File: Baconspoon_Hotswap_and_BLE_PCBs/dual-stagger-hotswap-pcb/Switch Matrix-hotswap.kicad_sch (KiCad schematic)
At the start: 87 parts

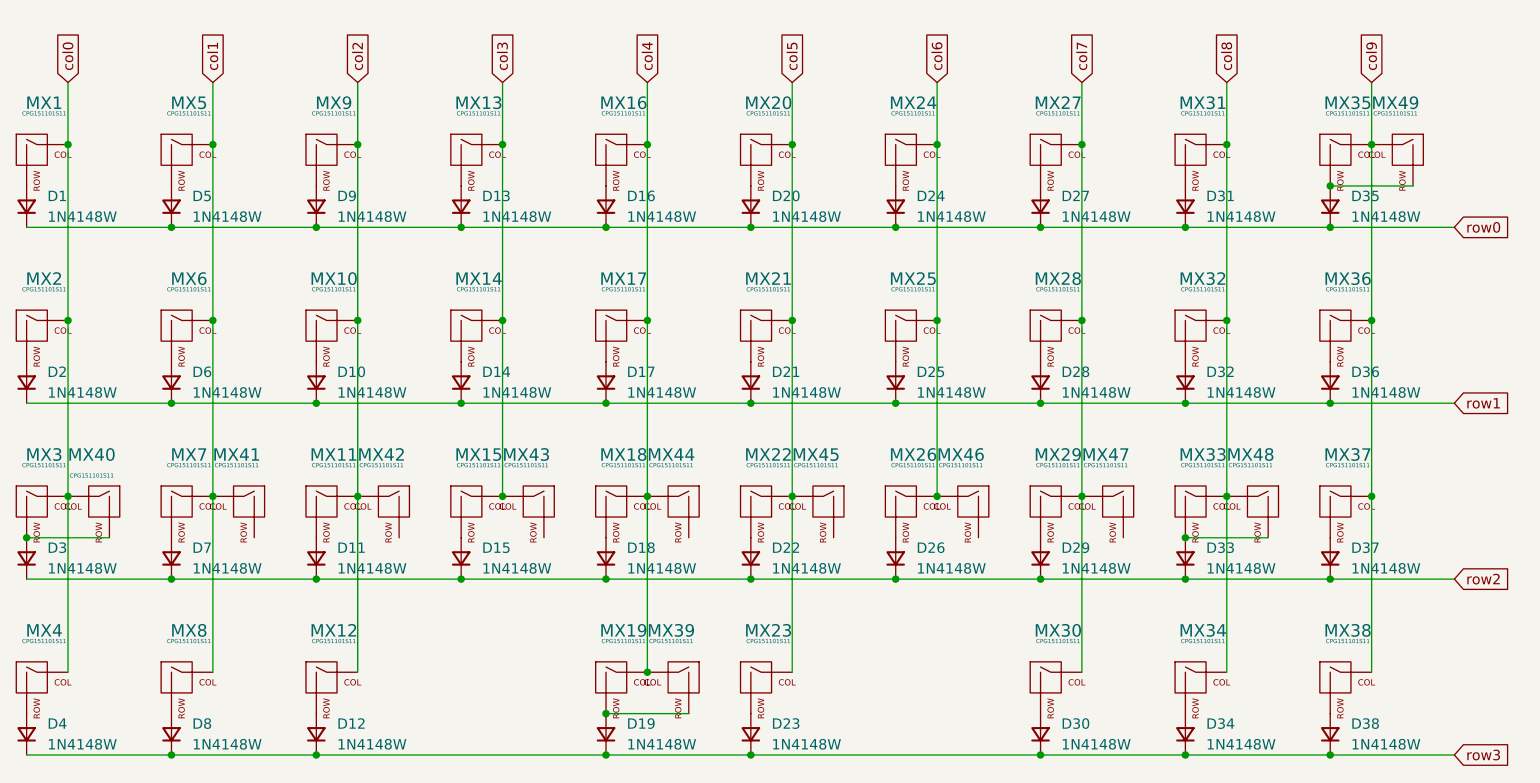
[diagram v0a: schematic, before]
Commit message: upload accurate fabrication files for dual-stagger hotswap PCB
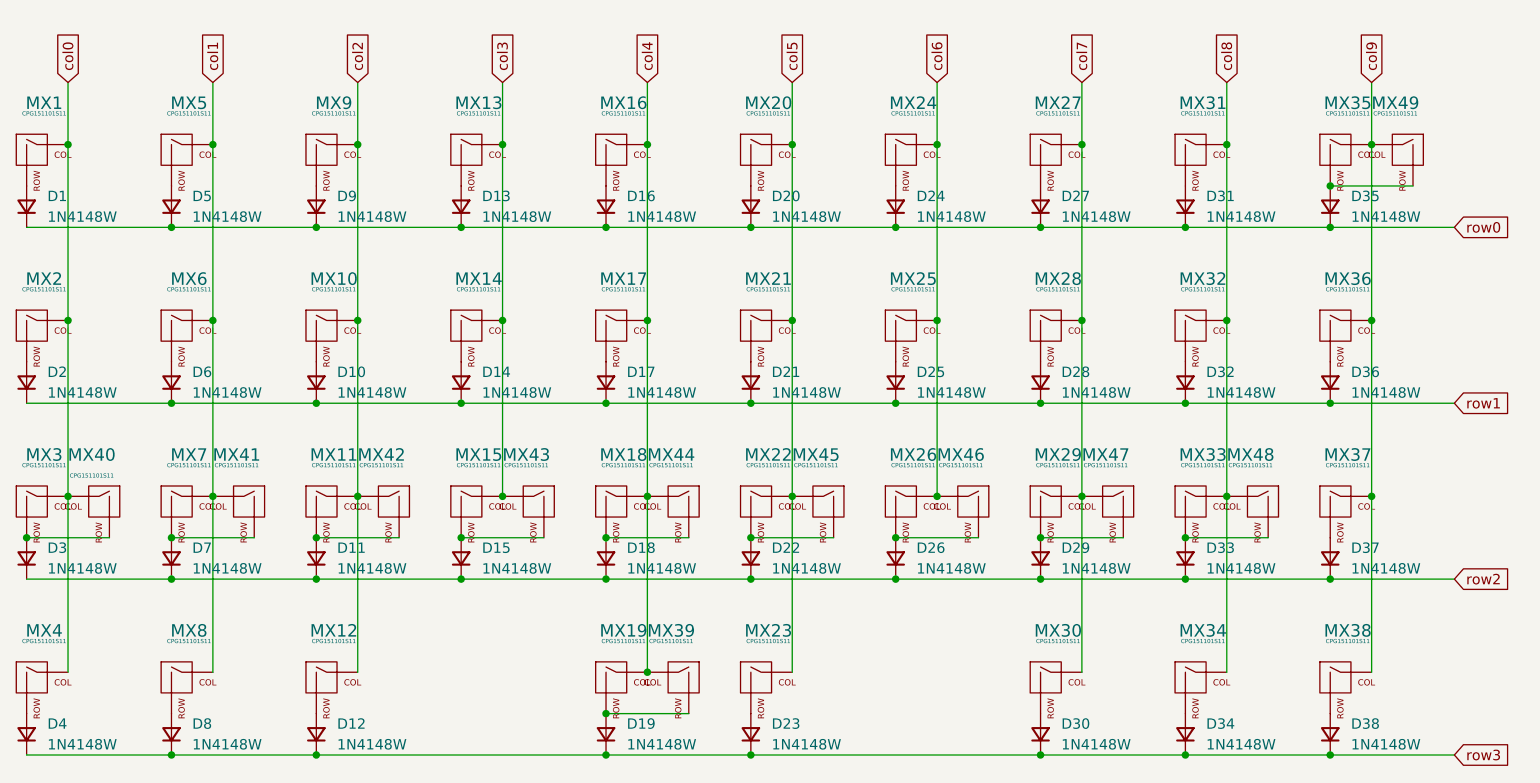
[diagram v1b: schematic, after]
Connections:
- net at D11.2 (A), MX11.2 (ROW): now also MX42.2 (ROW)
- net at D18.2 (A), MX18.2 (ROW): now also MX44.2 (ROW)
- net at D26.2 (A), MX26.2 (ROW): now also MX46.2 (ROW)
- net at MX47.2 (ROW): now also D29.2 (A), MX29.2 (ROW)
- net at MX41.2 (ROW): now also D7.2 (A), MX7.2 (ROW)
- net at D22.2 (A), MX22.2 (ROW): now also MX45.2 (ROW)
- net at MX43.2 (ROW): now also D15.2 (A), MX15.2 (ROW)
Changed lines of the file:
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@@
   (junction (at 151.13 54.61) (diameter 0) (color 0 0 0 0)
   )
+  (junction (at 62.23 92.71) (diameter 0) (color 0 0 0 0)
+  )
   (junction (at 151.13 97.79) (diameter 0) (color 0 0 0 0)
   )
@@
   (junction (at 173.99 66.04) (diameter 0) (color 0 0 0 0)
   )
+  (junction (at 133.35 92.71) (diameter 0) (color 0 0 0 0)
+  )
   (junction (at 115.57 119.38) (diameter 0) (color 0 0 0 0)
   )
+  (junction (at 97.79 92.71) (diameter 0) (color 0 0 0 0)
+  )
   (junction (at 209.55 87.63) (diameter 0) (color 0 0 0 0)
   )
@@
   (junction (at 204.47 97.79) (diameter 0) (color 0 0 0 0)
   )
+  (junction (at 168.91 92.71) (diameter 0) (color 0 0 0 0)
+  )
   (junction (at 191.77 66.04) (diameter 0) (color 0 0 0 0)
   )
@@
   (junction (at 80.01 97.79) (diameter 0) (color 0 0 0 0)
   )
+  (junction (at 115.57 92.71) (diameter 0) (color 0 0 0 0)
+  )
   (junction (at 102.87 44.45) (diameter 0) (color 0 0 0 0)
   )
@@
   (junction (at 186.69 92.71) (diameter 0) (color 0 0 0 0)
   )
+  (junction (at 80.01 92.71) (diameter 0) (color 0 0 0 0)
+  )
+  (junction (at 151.13 92.71) (diameter 0) (color 0 0 0 0)
+  )
   (wire (pts (xy 120.65 44.45) (xy 120.65 66.04))
     (stroke (width 0) (type default))
@@
     (stroke (width 0) (type default))
   )
+  (wire (pts (xy 62.23 92.71) (xy 72.39 92.71))
+    (stroke (width 0) (type default))
+  )
   (wire (pts (xy 49.53 66.04) (xy 49.53 87.63))
     (stroke (width 0) (type default))
@@
     (stroke (width 0) (type default))
   )
+  (wire (pts (xy 97.79 92.71) (xy 107.95 92.71))
+    (stroke (width 0) (type default))
+  )
   (wire (pts (xy 67.31 66.04) (xy 67.31 87.63))
     (stroke (width 0) (type default))
@@
     (stroke (width 0) (type default))
   )
+  (wire (pts (xy 80.01 92.71) (xy 90.17 92.71))
+    (stroke (width 0) (type default))
+  )
   (wire (pts (xy 85.09 87.63) (xy 85.09 109.22))
     (stroke (width 0) (type default))
@@
     (stroke (width 0) (type default))
   )
+  (wire (pts (xy 168.91 92.71) (xy 179.07 92.71))
+    (stroke (width 0) (type default))
+  )
   (wire (pts (xy 85.09 44.45) (xy 85.09 66.04))
     (stroke (width 0) (type default))
@@
     (stroke (width 0) (type default))
   )
+  (wire (pts (xy 133.35 92.71) (xy 143.51 92.71))
+    (stroke (width 0) (type default))
+  )
   (wire (pts (xy 219.71 76.2) (xy 204.47 76.2))
     (stroke (width 0) (type default))
@@
     (stroke (width 0) (type default))
   )
+  (wire (pts (xy 151.13 92.71) (xy 161.29 92.71))
+    (stroke (width 0) (type default))
+  )
   (wire (pts (xy 151.13 76.2) (xy 133.35 76.2))
     (stroke (width 0) (type default))
@@
     (stroke (width 0) (type default))
   )
+  (wire (pts (xy 115.57 92.71) (xy 125.73 92.71))
+    (stroke (width 0) (type default))
+  )
